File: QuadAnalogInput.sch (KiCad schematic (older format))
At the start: 22 parts, among them U201 LM324

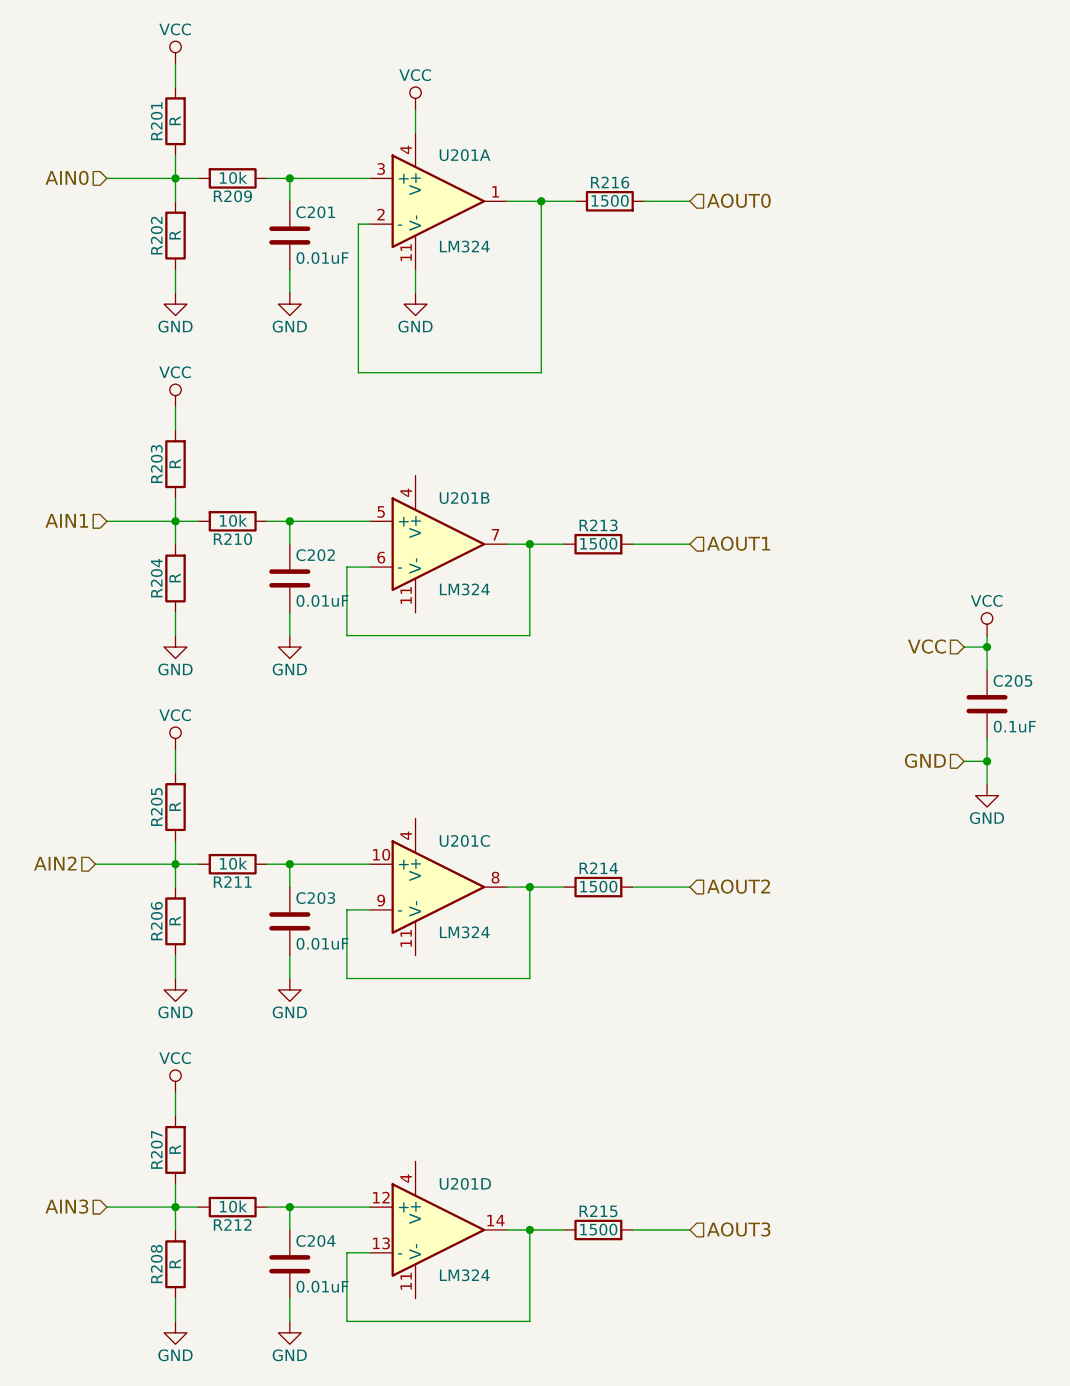
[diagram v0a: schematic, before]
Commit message: Rework most of board for rusefi
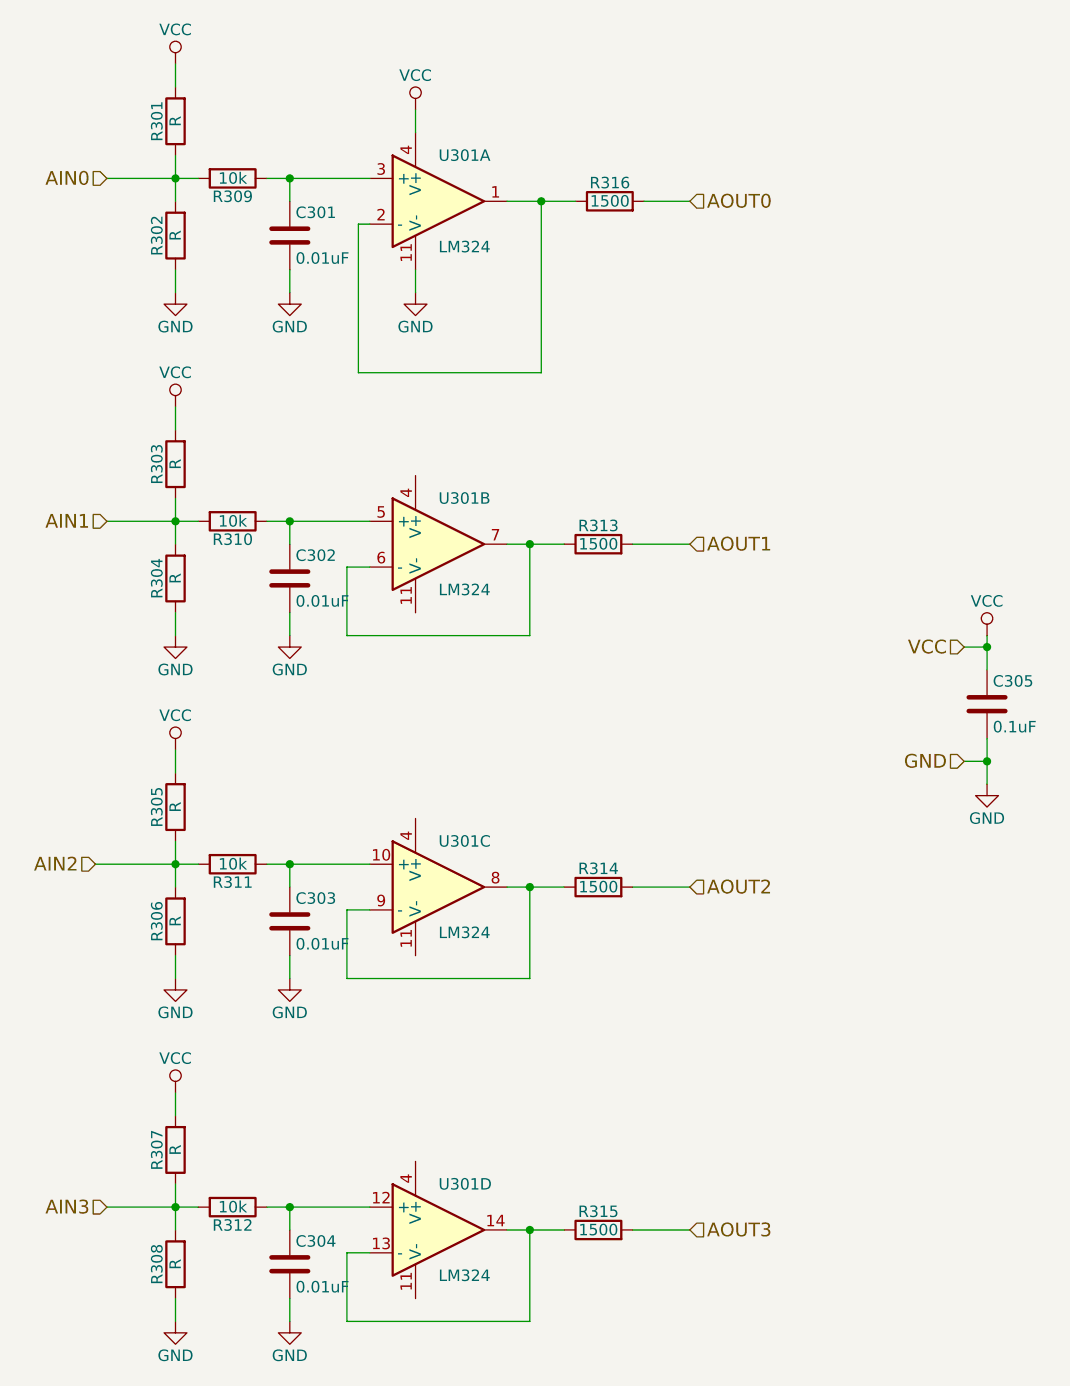
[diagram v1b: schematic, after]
